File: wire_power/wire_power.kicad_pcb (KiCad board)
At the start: 2 copper layers, 99 x 99 mm, 61 parts, among them J1 CONN_02X03, J10 Through_hole, J11 Through_hole, J12 Through_hole, J13 Through_hole, J14 Through_hole, J15 Through_hole, J16 Through_hole, J17 Through_hole, J18 Through_hole, J19 Through_hole, J2 CONN_02X03, J20 Through_hole, J21 Through_hole, J22 Through_hole, J23 Through_hole, J24 Through_hole, J25 Through_hole, J26 Through_hole, J27 Through_hole, J28 Through_hole, J29 Through_hole, J3 Through_hole, J30 Through_hole, J4 Through_hole, J5 Through_hole, J6 Through_hole, J7 Through_hole, J8 Through_hole, J9 Through_hole, Q1 CPC1025NTR, Q10 CPC1025NTR, Q11 CPC1025NTR, Q12 CPC1025NTR, Q13 CPC1025NTR, Q14 CPC1025NTR, Q15 CPC1025NTR, Q16 CPC1025NTR, Q17 CPC1025NTR, Q18 CPC1025NTR, Q19 CPC1025NTR, Q2 CPC1025NTR, Q20 CPC1025NTR, Q21 CPC1025NTR, Q22 CPC1025NTR, Q23 CPC1025NTR, Q24 CPC1025NTR, Q25 CPC1025NTR, Q26 CPC1025NTR, Q3 CPC1025NTR, Q4 CPC1025NTR, Q5 CPC1025NTR, Q6 CPC1025NTR, Q7 CPC1025NTR, Q8 CPC1025NTR, Q9 CPC1025NTR, U1 ADG732

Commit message: final pass at wire_power layout)
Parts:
- moved J30 43.9 mm to (112.7, 67.8)
- moved J3 3.02 mm to (158.6, 74.1)
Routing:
- net GND: track 26.4 -> 71.7 mm, vias 0 -> 26
- net /Hot_in: track 314.3 -> 336.0 mm
- added copper zone on B.Cu, net GND
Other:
- board text added: "A"
- board text added: "B"
- board text added: "C"
- board text added: "Corey Cochran-Lepiz Bryce Mann"
- board text added: "D"
- board text added: "Do not touch!"
- board text added: "E"
- board text added: "F"
- board text added: "G"
- board text added: "H"
- board text added: "I"
- board text added: "J"
- board text added: "K"
- board text added: "L"
- board text added: "M"
- board text added: "N"
- board text added: "O"
- board text added: "P"
- board text added: "Q"
- board text added: "R"
- board text added: "S"
- board text added: "T"
- board text added: "Team Enigma Principles of Engineering Fall 2018"
- board text added: "U"
- board text added: "V"
- board text added: "W"
- board text added: "X"
- board text added: "Y"
- board text added: "Z"

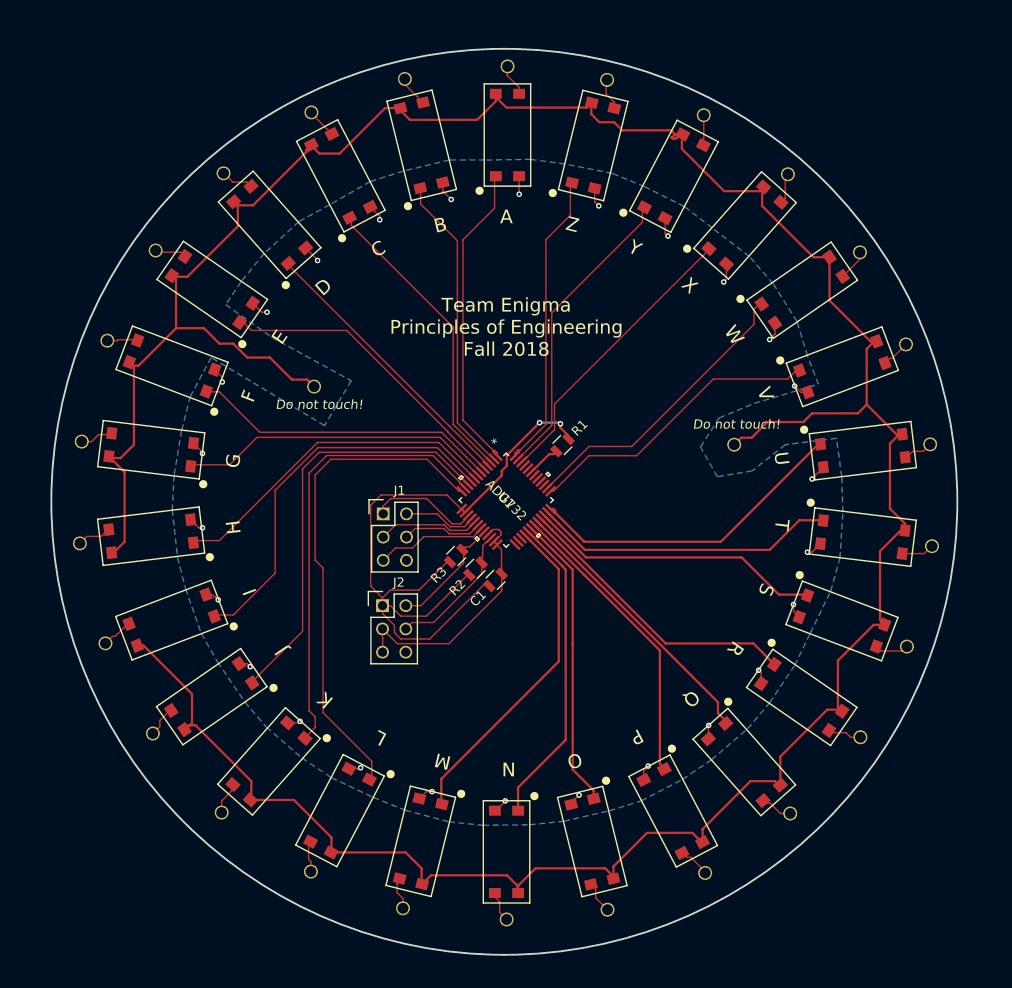
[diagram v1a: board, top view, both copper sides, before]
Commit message: Revised final pass of wire_power layout
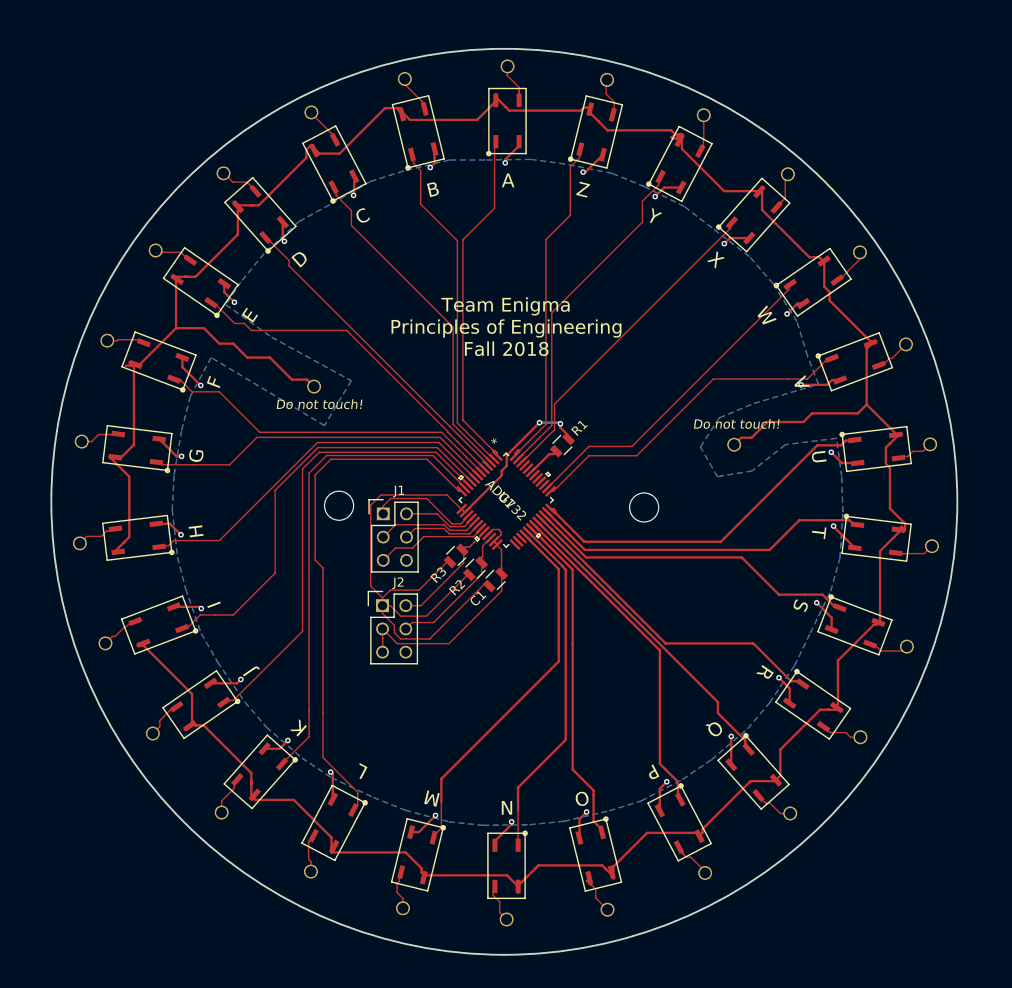
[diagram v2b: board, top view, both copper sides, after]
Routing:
- net GND: track 71.7 -> 107.2 mm
- net /SY: track 32.8 -> 37.1 mm
- net /SZ: track 32.2 -> 36.5 mm
- net /SV: track 32.6 -> 36.5 mm
- net /SJ: track 45.6 -> 49.5 mm
- net /SE: track 33.0 -> 36.9 mm
- net /SU: track 35.1 -> 39.0 mm
- net /SH: track 36.5 -> 40.4 mm
- net /SF: track 33.5 -> 37.3 mm
- net /SO: track 32.0 -> 35.8 mm
- net /SB: track 32.8 -> 36.6 mm
- net /SM: track 36.1 -> 39.9 mm
- net /SD: track 30.8 -> 34.6 mm
- net /SC: track 32.9 -> 36.6 mm
- net /SI: track 42.4 -> 46.2 mm
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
